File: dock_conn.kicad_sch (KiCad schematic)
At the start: 31 parts, among them J10 Conn_02x35_Odd_Even

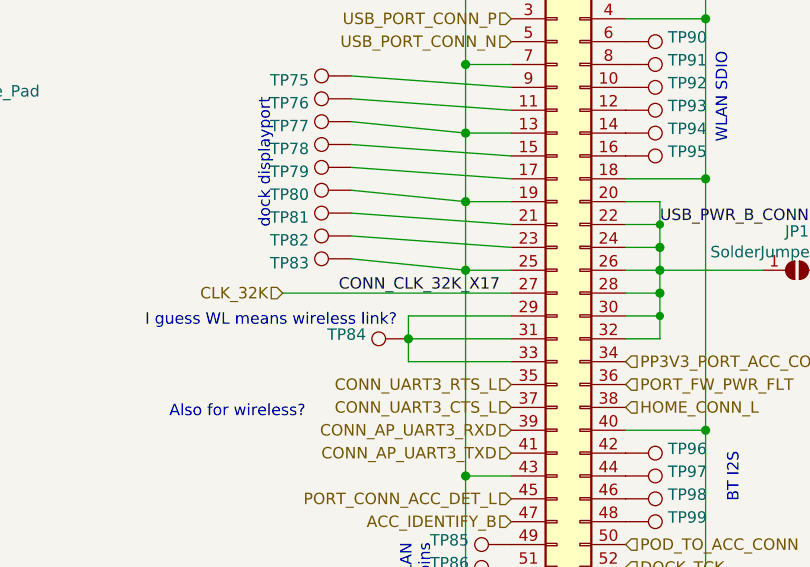
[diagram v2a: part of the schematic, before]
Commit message: Fix most ERC errors; cleanup silkscreen and comment layers.
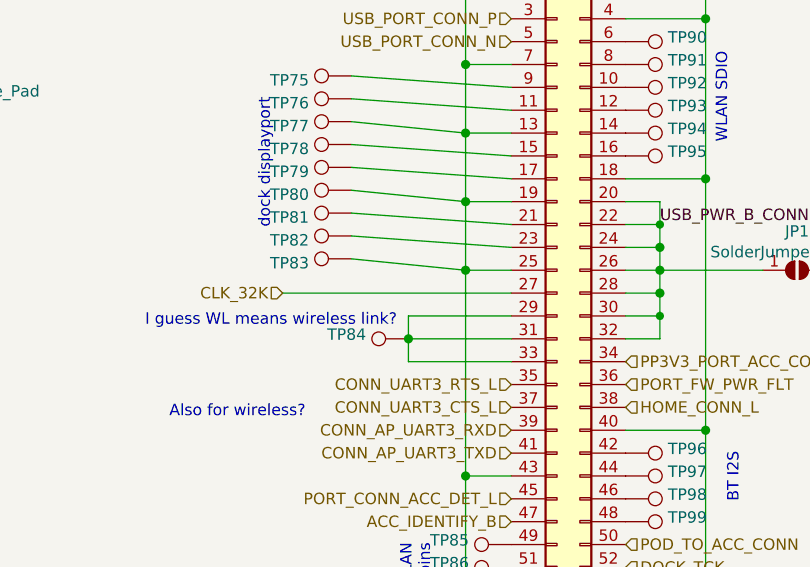
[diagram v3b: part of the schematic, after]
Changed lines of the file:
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@@
     (effects (font (size 1.27 1.27)) (justify left bottom))
-  )
-  (label "CONN_CLK_32K_X17" (at 130.81 80.01 180)
-    (effects (font (size 1.27 1.27)) (justify right bottom))
   )
   (hierarchical_label "PORT_FW_PWR_FLT" (shape input) (at 144.78 90.17 0)

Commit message: Board rev2 ready to order, hopefully
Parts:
- added TP115: TestPoint, footprints:testpoint_small, symbol Connector:TestPoint
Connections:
- net GND: now also TP115.1
